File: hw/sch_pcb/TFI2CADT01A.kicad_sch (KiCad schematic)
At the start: 31 parts, among them J1 SM04B-GHS-TB, J2 SM04B-GHS-TB, J3 SM04B-GHS-TB, J4 SM04B-GHS-TB, M1 HOLE, M2 HOLE, M3 HOLE, M4 HOLE, M5 HOLE, M6 HOLE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

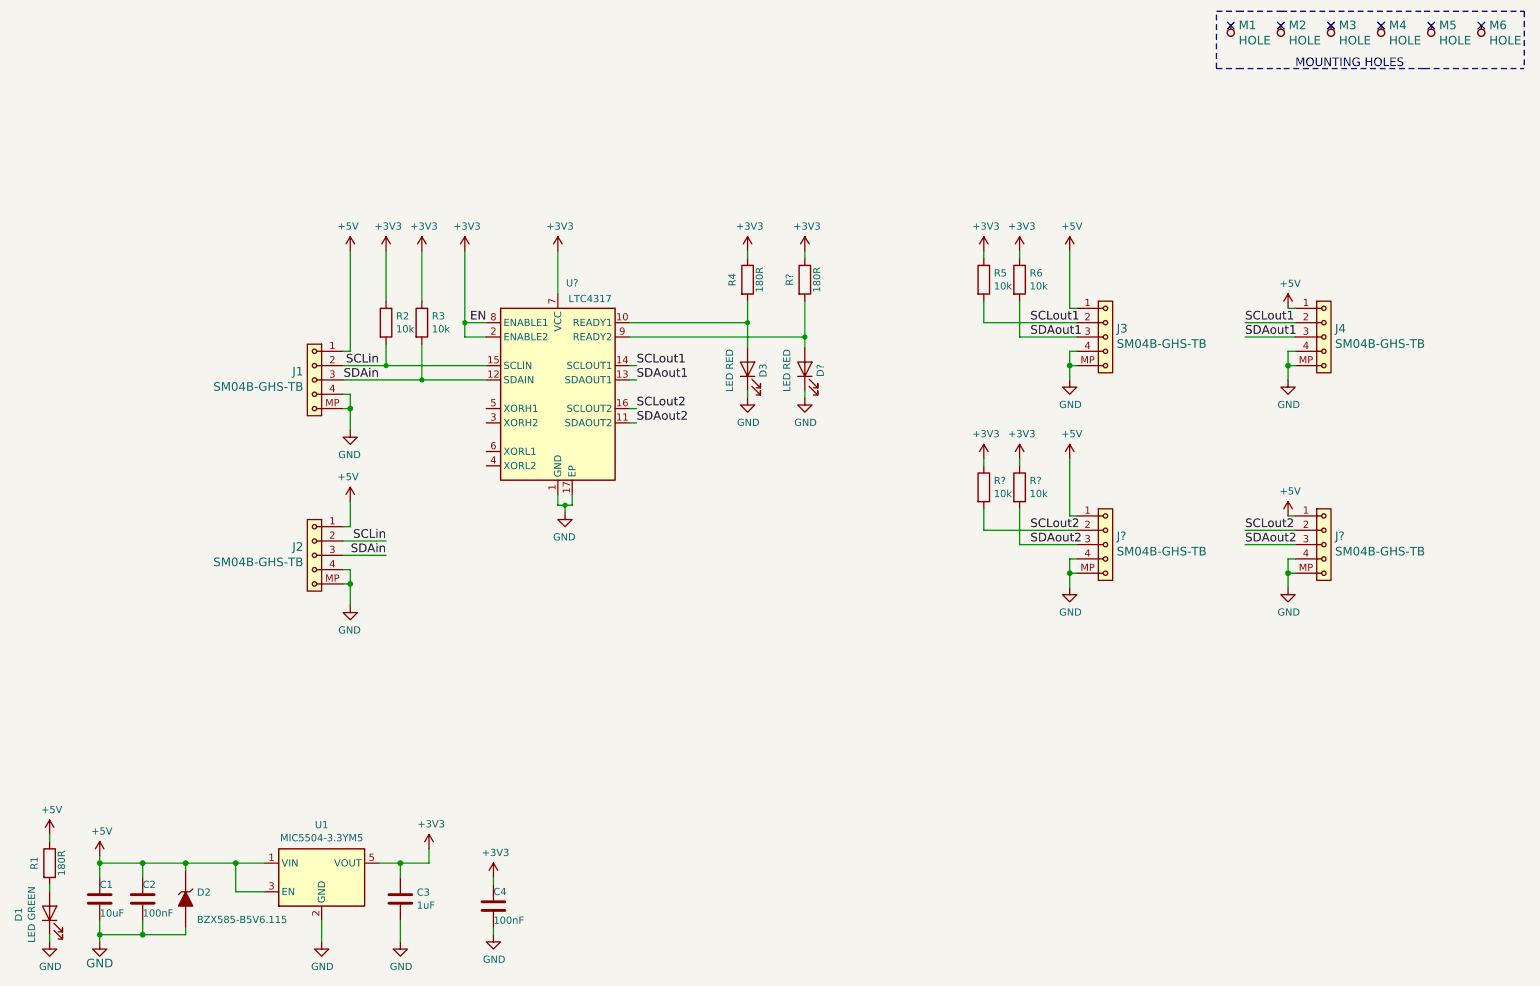
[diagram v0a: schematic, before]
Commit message: volba adres rezistory
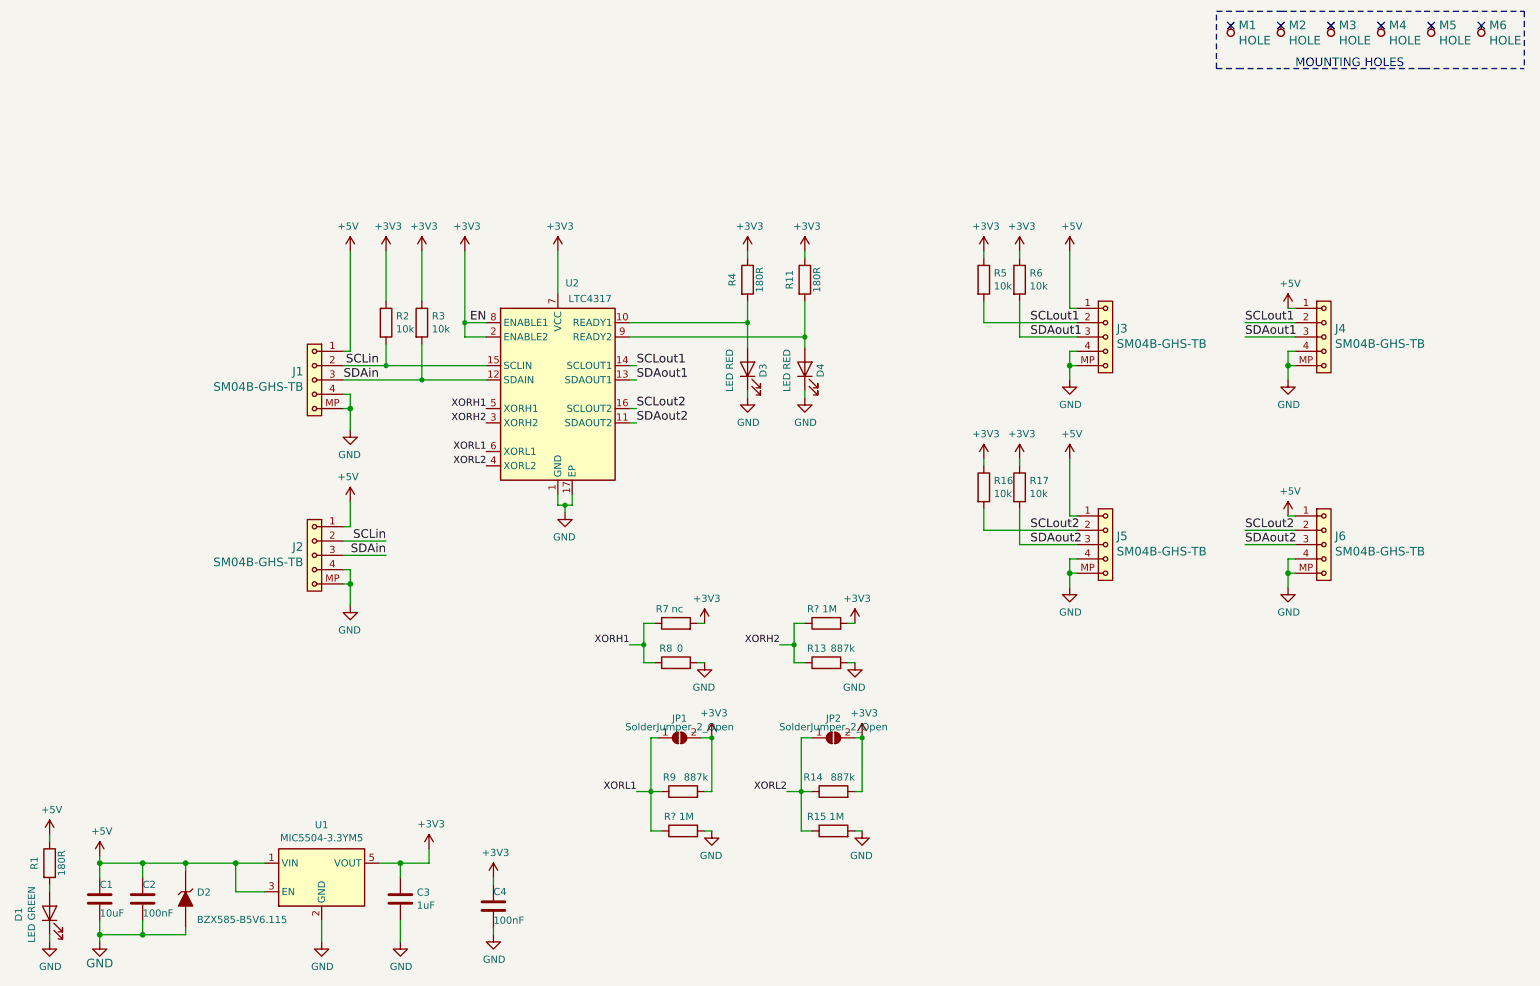
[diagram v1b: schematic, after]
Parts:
- added JP1, JP2: SolderJumper_2_Open, Jumper:SolderJumper-2_P1.3mm_Open_RoundedPad1.0x1.5mm, symbol Jumper:SolderJumper_2_Open
- added R13, R14, R9: 887k, symbol Device:R
- added R15, R? (x2): 1M, symbol Device:R
- added R7: nc, symbol Device:R
- added R8: 0, symbol Device:R
- gave numbers to parts that had none: 7
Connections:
- net +3V3: now also JP1.2 (B), JP2.2 (B), R14.2, R7.2, R9.2, R?.2
- net GND: now also R13.2, R15.2, R8.2, R?.2
- net XORH2: now reaches U2.3 (XORH2)
- net XORH2: now also R13.1, R?.1
- net XORL2: now reaches U2.4 (XORL2)
- net XORL2: now also JP2.1 (A), R14.1, R15.1
- net XORH1: now reaches U2.5 (XORH1)
- net XORH1: now also R7.1, R8.1
- net XORL1: now reaches U2.6 (XORL1)
- net XORL1: now also JP1.1 (A), R9.1, R?.1

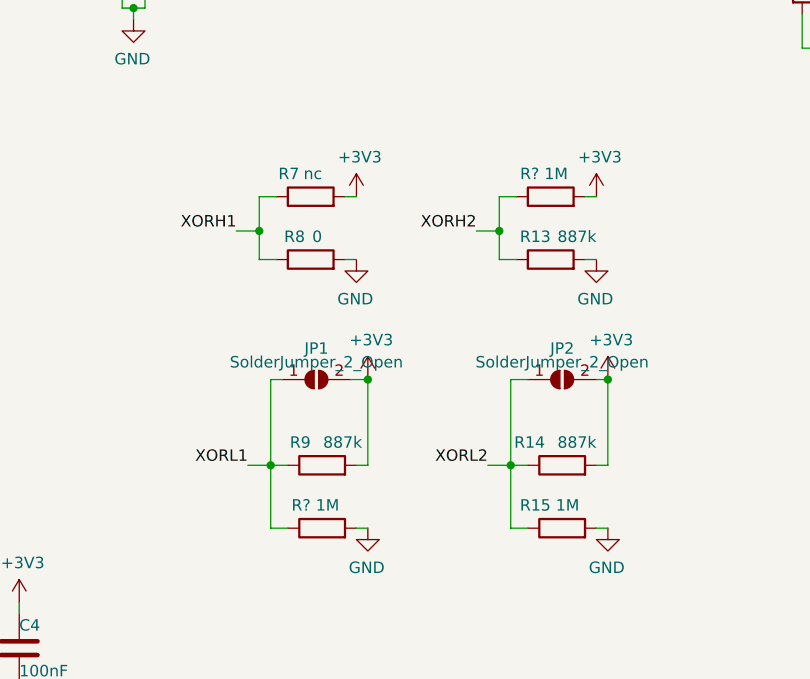
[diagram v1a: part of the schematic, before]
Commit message: anotace soucastek
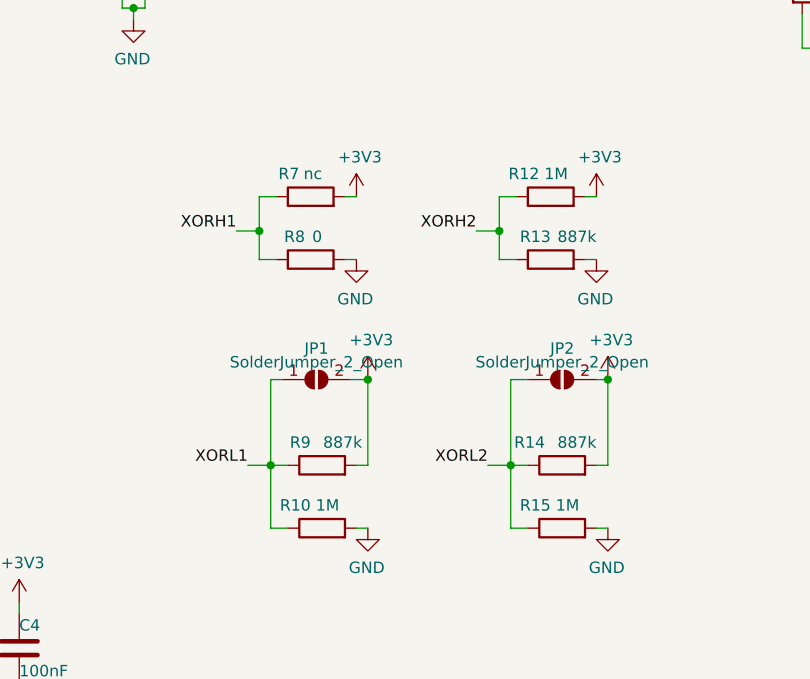
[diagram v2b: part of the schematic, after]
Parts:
- gave numbers to parts that had none: 2
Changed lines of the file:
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@@
   (symbol (lib_id "Device:R") (at 156.845 126.365 90) (unit 1)
     (in_bom yes) (on_board yes)
-    (property "Reference" "R?" (id 0) (at 155.575 123.825 90)
+    (property "Reference" "R12" (id 0) (at 155.575 123.825 90)
       (effects (font (size 1.27 1.27)) (justify left))
     )
@@
   (symbol (lib_id "Device:R") (at 131.445 163.195 90) (unit 1)
     (in_bom yes) (on_board yes)
-    (property "Reference" "R?" (id 0) (at 130.175 160.655 90)
+    (property "Reference" "R10" (id 0) (at 130.175 160.655 90)
       (effects (font (size 1.27 1.27)) (justify left))
     )
@@
       (reference "R9") (unit 1) (value "887k") (footprint "")
     )
+    (path "/ecd17538-5422-4aa3-9951-3654d3d4054e"
+      (reference "R10") (unit 1) (value "1M") (footprint "")
+    )
     (path "/63118696-0cad-41c6-bec2-fb8df2bc487f"
       (reference "R11") (unit 1) (value "180R") (footprint "Mlab_R:SMD-0603")
     )
+    (path "/4cfea622-e15b-484a-a2aa-621961cf6026"
+      (reference "R12") (unit 1) (value "1M") (footprint "")
+    )
     (path "/e522d3ba-c528-466d-97f7-febc1fe1663f"
       (reference "R13") (unit 1) (value "887k") (footprint "")
@@
       (reference "R17") (unit 1) (value "10k") (footprint "Mlab_R:SMD-0603")
     )
-    (path "/4cfea622-e15b-484a-a2aa-621961cf6026"
-      (reference "R?") (unit 1) (value "1M") (footprint "")
-    )
-    (path "/ecd17538-5422-4aa3-9951-3654d3d4054e"
-      (reference "R?") (unit 1) (value "1M") (footprint "")
-    )
     (path "/00000000-0000-0000-0000-00005de928cf"

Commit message: Edit PCB
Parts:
- removed D3, D4: LED RED, Mlab_D:LED_1206, symbol Device:LED
- removed R11, R4: 180R, Mlab_R:SMD-0603, symbol Device:R
- C1: footprint Mlab_R:SMD-0805 -> Capacitor_SMD:C_0805_2012Metric
- C2, C3, C4: footprint Mlab_R:SMD-0603 -> Capacitor_SMD:C_0603_1608Metric
- D1: footprint Mlab_D:LED_1206 -> LED_SMD:LED_0603_1608Metric
- M1, M2, M3, M4, M5, M6: symbol MLAB_MECHANICAL:HOLE -> MLAB_MECHANICAL:HOLE_TF
- R1, R16, R17, R2, R3, R5, R6: footprint Mlab_R:SMD-0603 -> Resistor_SMD:R_0603_1608Metric
- R10, R12, R13, R14, R15, R9: footprint (none) -> Resistor_SMD:R_0603_1608Metric
- R7: value nc -> -; footprint (none) -> Resistor_SMD:R_0603_1608Metric
- R8: value 0 -> 180R; footprint (none) -> Resistor_SMD:R_0603_1608Metric
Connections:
- net GND: now also U2.10 (READY1), U2.9 (READY2)
- no-connect marks 6 -> 0

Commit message: uprava routingu
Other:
- note added: "Address XOR translations: Output 1: Open - 0x08 Shorted - 0x0f Output 2: Open - 0x78 Shorted - 0x7f"
- moved on the sheet: C1, C2, C3, C4, D1, D2, R1, U1

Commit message: Edit PCB
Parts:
- added G1: LOGO, MLAB_LOGA:TF 10x4,7, symbol MLAB_TF_LOGO:LOGO
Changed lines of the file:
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@@
     (pin "2")
+  )
+  (symbol (lib_id "MLAB_TF_LOGO:LOGO") (at 267.335 156.845 0) (unit 1)
+    (in_bom no) (on_board yes)
+    (property "Reference" "G1" (id 0) (at 254 151.13 0)
+      (effects (font (size 1.27 1.27)) (justify left))
+    )
+    (property "Value" "LOGO" (id 1) (at 267.335 163.3126 0)
+      (effects (font (size 1.27 1.27)) hide)
+    )
+    (property "Footprint" "MLAB_LOGA:TF 10x4,7" (id 2) (at 267.335 156.845 0)
+      (effects (font (size 1.27 1.27)) hide)
+    )
+    (property "Datasheet" "" (id 3) (at 267.335 156.845 0)
+      (effects (font (size 1.27 1.27)) hide)
+    )
   )
   (symbol (lib_id "Jumper:SolderJumper_2_Open") (at 130.81 146.685 0) (unit 1)
@@
     (pin "2")
   )
-  (symbol (lib_id "MLAB_MECHANICAL:HOLE_TF") (at 273.05 21.59 90) (unit 1)
+  (symbol (lib_name "HOLE_TF_5") (lib_id "MLAB_MECHANICAL:HOLE_TF") (at 273.05 21.59 90) (unit 1)
     (in_bom yes) (on_board yes) (fields_autoplaced)
     (property "Reference" "M6" (id 0) (at 274.4471 20.2579 90)
@@
     (pin "1")
   )
-  (symbol (lib_id "MLAB_MECHANICAL:HOLE_TF") (at 255.27 21.59 90) (unit 1)
+  (symbol (lib_name "HOLE_TF_2") (lib_id "MLAB_MECHANICAL:HOLE_TF") (at 255.27 21.59 90) (unit 1)
     (in_bom yes) (on_board yes) (fields_autoplaced)
     (property "Reference" "M4" (id 0) (at 256.6671 20.2579 90)
@@
     (pin "1")
   )
-  (symbol (lib_id "MLAB_MECHANICAL:HOLE_TF") (at 246.38 21.59 90) (unit 1)
+  (symbol (lib_name "HOLE_TF_3") (lib_id "MLAB_MECHANICAL:HOLE_TF") (at 246.38 21.59 90) (unit 1)
     (in_bom yes) (on_board yes)
     (property "Reference" "M3" (id 0) (at 247.7771 20.2579 90)
@@
     (pin "1")
   )
-  (symbol (lib_id "MLAB_MECHANICAL:HOLE_TF") (at 237.49 21.59 90) (unit 1)
+  (symbol (lib_name "HOLE_TF_4") (lib_id "MLAB_MECHANICAL:HOLE_TF") (at 237.49 21.59 90) (unit 1)
     (in_bom yes) (on_board yes) (fields_autoplaced)
     (property "Reference" "M2" (id 0) (at 238.8871 20.2579 90)
@@
     (pin "2")
   )
-  (symbol (lib_id "MLAB_MECHANICAL:HOLE_TF") (at 228.6 21.59 90) (unit 1)
+  (symbol (lib_name "HOLE_TF_1") (lib_id "MLAB_MECHANICAL:HOLE_TF") (at 228.6 21.59 90) (unit 1)
     (in_bom yes) (on_board yes) (fields_autoplaced)
     (property "Reference" "M1" (id 0) (at 229.9971 20.2579 90)
@@
       (reference "D2") (unit 1) (value "BZX585-B5V6.115") (footprint "Diode_SMD:D_SOD-523")
     )
+    (path "/0e440c09-c0c0-468b-ade3-d3b3f920f815"
+      (reference "G1") (unit 1) (value "LOGO") (footprint "MLAB_LOGA:TF 10x4,7")
+    )
     (path "/00000000-0000-0000-0000-00005de8841c"

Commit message: Edit pcb
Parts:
- D1: UST_ID 5c70984412875079b91f8895 -> 60d582331287500165f859d0
- R10, R12, R15: UST_ID (none) -> 61e030ee2eac0c9aef5c8995
- R13, R14, R9: UST_ID (none) -> 61e02cad2eac0c9aef5c894c
- R8: UST_ID (none) -> 5c70984512875079b91f8957
- U2: UST_ID (none) -> 61e031592eac0c9aef5c89ad
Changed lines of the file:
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@@
       (effects (font (size 1.27 1.27)) hide)
     )
-    (property "UST_ID" "" (id 5) (at 131.445 156.21 0)
+    (property "UST_ID" "61e02cad2eac0c9aef5c894c" (id 5) (at 131.445 156.21 0)
       (effects (font (size 1.27 1.27)) hide)
     )
@@
       (effects (font (size 1.27 1.27)) hide)
     )
-    (property "UST_ID" "" (id 5) (at 130.175 133.35 0)
+    (property "UST_ID" "5c70984512875079b91f8957" (id 5) (at 130.175 133.35 0)
       (effects (font (size 1.27 1.27)) hide)
     )
@@
     )
     (property "Datasheet" "https://www.analog.com/media/en/technical-documentation/data-sheets/4317fa.pdf" (id 3) (at 93.98 43.815 0)
+      (effects (font (size 1.27 1.27)) hide)
+    )
+    (property "UST_ID" "61e031592eac0c9aef5c89ad" (id 4) (at 109.22 85.725 0)
       (effects (font (size 1.27 1.27)) hide)
     )
@@
       (effects (font (size 1.27 1.27)) hide)
     )
-    (property "UST_ID" "" (id 5) (at 156.845 126.365 0)
+    (property "UST_ID" "61e030ee2eac0c9aef5c8995" (id 5) (at 156.845 126.365 0)
       (effects (font (size 1.27 1.27)) hide)
     )
@@
       (effects (font (size 1.27 1.27)) hide)
     )
-    (property "UST_ID" "" (id 5) (at 158.115 163.195 0)
+    (property "UST_ID" "61e030ee2eac0c9aef5c8995" (id 5) (at 158.115 163.195 0)
       (effects (font (size 1.27 1.27)) hide)
     )
@@
       (effects (font (size 1.27 1.27)) hide)
     )
-    (property "UST_ID" "5c70984412875079b91f8895" (id 5) (at 31.75 175.26 0)
+    (property "UST_ID" "60d582331287500165f859d0" (id 5) (at 31.75 175.26 0)
       (effects (font (size 1.27 1.27)) hide)
     )
@@
       (effects (font (size 1.27 1.27)) hide)
     )
-    (property "UST_ID" "" (id 5) (at 158.115 156.21 0)
+    (property "UST_ID" "61e02cad2eac0c9aef5c894c" (id 5) (at 158.115 156.21 0)
       (effects (font (size 1.27 1.27)) hide)
     )
@@
       (effects (font (size 1.27 1.27)) hide)
     )
-    (property "UST_ID" "" (id 5) (at 156.845 133.35 0)
+    (property "UST_ID" "61e02cad2eac0c9aef5c894c" (id 5) (at 156.845 133.35 0)
       (effects (font (size 1.27 1.27)) hide)
     )
@@
       (effects (font (size 1.27 1.27)) hide)
     )
-    (property "UST_ID" "" (id 5) (at 131.445 163.195 0)
-      (effects (font (size 1.27 1.27)) hide)
-    )
+    (property "UST_ID" "61e030ee2eac0c9aef5c8995" (id 5) (at 131.445 163.195 0)
+      (effects (font (size 1.27 1.27)) hide)
+    )
